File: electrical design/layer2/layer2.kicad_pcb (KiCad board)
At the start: 2 copper layers, 178 x 168.1 mm, 47 parts, among them J1 Conn_01x01_Female, J10 Conn_01x01_Female, J11 SH1.0 3P, J12 XH2.54 3P, J13 XT60-F, J14 XH2.54 2P, J15 XT60-F, J16 XT60-F, J17 SH1.0 2P, J18 Conn_01x01_Female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

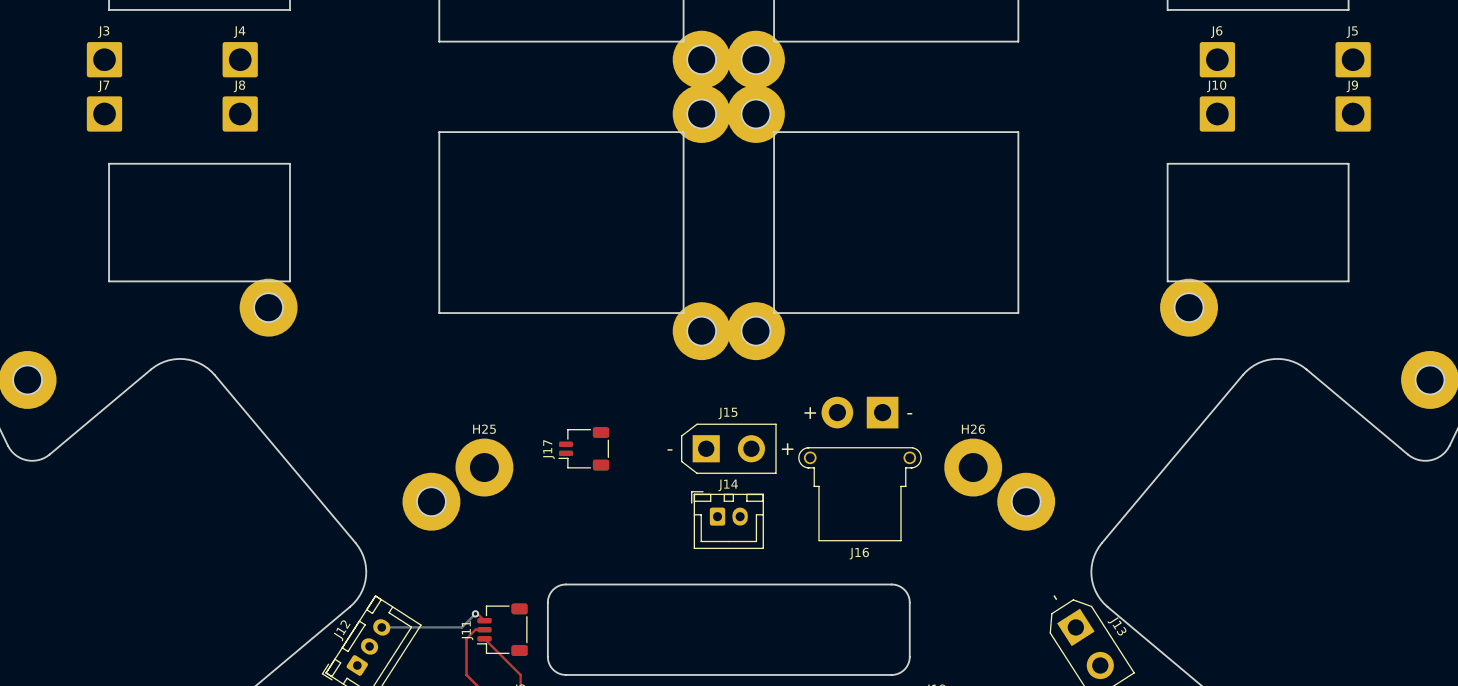
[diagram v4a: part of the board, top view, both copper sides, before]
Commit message: add pwm pullup resistor to rpi fan connector
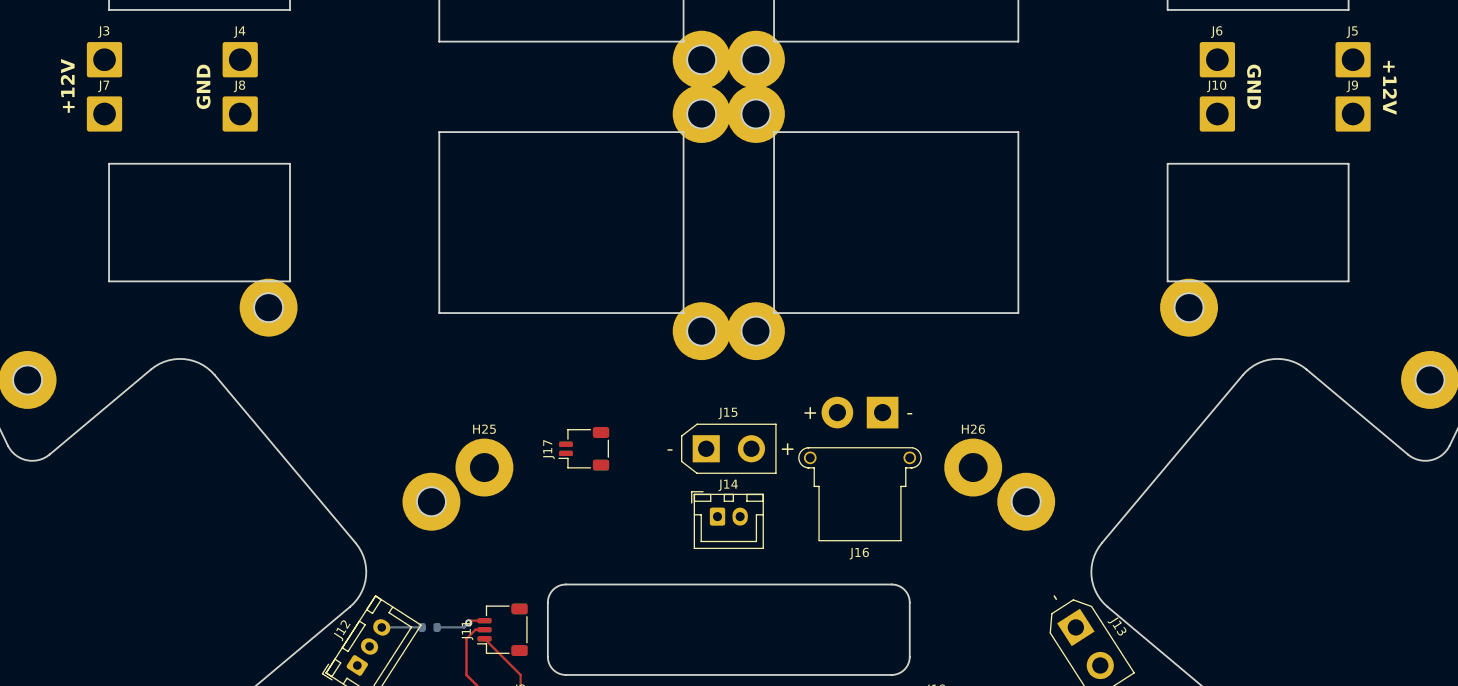
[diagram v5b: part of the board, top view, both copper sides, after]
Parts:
- added R1: 10k, Resistor_SMD:R_0603_1608Metric, B.Cu at (71.9, 164.8)
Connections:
- J12 pad 3: +3V3 -> Net-(J12-Pin_3)
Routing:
- net +3V3: track 12.3 -> 6.26 mm
- net Net-(J12-Pin_3): track 0.00 -> 4.46 mm
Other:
- board text added: "+12V"
- board text added: "GND"
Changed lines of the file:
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@@
   (net 3 "/BATT")
   (net 4 "+3V3")
+  (net 5 "Net-(J12-Pin_3)")
   (footprint "Connector_AMASS:AMASS_XT30UPB-F_1x02_P5.0mm_Vertical" (layer "F.Cu")
     (at 143.357043 164.747279 -57.3)
@@
       (net 1 "+12V") (pinfunction "Pin_2") (pintype "passive"))
     (pad "3" thru_hole oval (at 5 0 57.301) (size 1.7 1.95) (drill 0.95) (layers "*.Cu" "*.Mask")
-      (net 4 "+3V3") (pinfunction "Pin_3") (pintype "passive"))
+      (net 5 "Net-(J12-Pin_3)") (pinfunction "Pin_3") (pintype "passive"))
     (model "${KICAD6_3DMODEL_DIR}/Connector_JST.3dshapes/JST_XH_B3B-XH-A_1x03_P2.50mm_Vertical.wrl"
       (offset (xyz 0 0 0))
@@
     )
   )
+  (footprint "Resistor_SMD:R_0603_1608Metric" (layer "B.Cu")
+    (at 71.925 164.75)
+    (descr "Resistor SMD 0603 (1608 Metric), square (rectangular) end terminal, IPC_7351 nominal, (Body size source: IPC-SM-782 page 72, https://www.pcb-3d.com/wordpress/wp-content/uploads/ipc-sm-782a_amendment_1_and_2.pdf), generated with kicad-footprint-generator")
+    (tags "resistor")
+    (property "Sheetfile" "layer2.kicad_sch")
+    (property "Sheetname" "")
+    (property "ki_description" "Resistor")
+    (property "ki_keywords" "R res resistor")
+    (attr smd)
+    (fp_text reference "R1" (at 0 1.43) (layer "B.SilkS")
+        (effects (font (size 1 1) (thickness 0.15)) (justify mirror))
+    )
+    (fp_text value "10k" (at 0 -1.43) (layer "B.SilkS")
+        (effects (font (size 1 1) (thickness 0.15)) (justify mirror))
+    )
+    (fp_text user "${REFERENCE}" (at 0 0) (layer "B.Fab")
+        (effects (font (size 0.4 0.4) (thickness 0.06)) (justify mirror))
+    )
+    (fp_line (start -0.237258 -0.5225) (end 0.237258 -0.5225)
+      (stroke (width 0.12) (type solid)) (layer "B.SilkS"))
+    (fp_line (start -0.237258 0.5225) (end 0.237258 0.5225)
+      (stroke (width 0.12) (type solid)) (layer "B.SilkS"))
+    (fp_line (start -1.48 -0.73) (end -1.48 0.73)
+      (stroke (width 0.05) (type solid)) (layer "B.CrtYd"))
+    (fp_line (start -1.48 0.73) (end 1.48 0.73)
+      (stroke (width 0.05) (type solid)) (layer "B.CrtYd"))
+    (fp_line (start 1.48 -0.73) (end -1.48 -0.73)
+      (stroke (width 0.05) (type solid)) (layer "B.CrtYd"))
+    (fp_line (start 1.48 0.73) (end 1.48 -0.73)
+      (stroke (width 0.05) (type solid)) (layer "B.CrtYd"))
+    (fp_line (start -0.8 -0.4125) (end -0.8 0.4125)
+      (stroke (width 0.1) (type solid)) (layer "B.Fab"))
+    (fp_line (start -0.8 0.4125) (end 0.8 0.4125)
+      (stroke (width 0.1) (type solid)) (layer "B.Fab"))
+    (fp_line (start 0.8 -0.4125) (end -0.8 -0.4125)
+      (stroke (width 0.1) (type solid)) (layer "B.Fab"))
+    (fp_line (start 0.8 0.4125) (end 0.8 -0.4125)
+      (stroke (width 0.1) (type solid)) (layer "B.Fab"))
+    (pad "1" smd roundrect (at -0.825 0) (size 0.8 0.95) (layers "B.Cu" "B.Paste" "B.Mask") (roundrect_rratio 0.25)
+      (net 5 "Net-(J12-Pin_3)") (pintype "passive"))
+    (pad "2" smd roundrect (at 0.825 0) (size 0.8 0.95) (layers "B.Cu" "B.Paste" "B.Mask") (roundrect_rratio 0.25)
+      (net 4 "+3V3") (pintype "passive"))
+    (model "${KICAD6_3DMODEL_DIR}/Resistor_SMD.3dshapes/R_0603_1608Metric.wrl"
+      (offset (xyz 0 0 0))
+      (scale (xyz 1 1 1))
+      (rotate (xyz 0 0 0))
+    )
+  )
   (gr_arc (start 25.330811 65.328595) (mid 27.404624 63.728825) (end 29.944652 64.3677)
     (stroke (width 0.2) (type solid)) (layer "Edge.Cuts"))
@@
   (gr_line (start 158.048228 171.859363) (end 146.853507 162.465877)
     (stroke (width 0.2) (type solid)) (layer "Edge.Cuts"))
+  (gr_text "GND" (at 47 105 90) (layer "F.SilkS")
+    (effects (font (size 1.5 1.5) (thickness 0.3) bold))
+  )
+  (gr_text "+12V" (at 32 105 90) (layer "F.SilkS")
+    (effects (font (size 1.5 1.5) (thickness 0.3) bold))
+  )
+  (gr_text "GND" (at 163 105 -90) (layer "F.SilkS")
+    (effects (font (size 1.5 1.5) (thickness 0.3) bold))
+  )
+  (gr_text "+12V" (at 178 105 -90) (layer "F.SilkS")
+    (effects (font (size 1.5 1.5) (thickness 0.3) bold))
+  )
   (segment (start 78 166) (end 82 170) (width 0.25) (layer "F.Cu") (net 2))
   (segment (start 78 165) (end 77 165) (width 0.25) (layer "F.Cu") (net 2))
@@
   (segment (start 76 170) (end 81 175) (width 0.25) (layer "F.Cu") (net 2))
   (segment (start 77 165) (end 76 166) (width 0.25) (layer "F.Cu") (net 2))
-  (segment (start 77 163.25) (end 77.25 163.25) (width 0.25) (layer "F.Cu") (net 4))
-  (segment (start 77.25 163.25) (end 78 164) (width 0.25) (layer "F.Cu") (net 4))
-  (via (at 77 163.25) (size 0.8) (drill 0.4) (layers "F.Cu" "B.Cu") (net 4))
-  (segment (start 66.642957 164.74728) (end 75.50272 164.74728) (width 0.25) (layer "B.Cu") (net 4))
-  (segment (start 75.50272 164.74728) (end 77 163.25) (width 0.25) (layer "B.Cu") (net 4))
+  (segment (start 78 164) (end 76.5 164) (width 0.25) (layer "F.Cu") (net 4))
+  (segment (start 76.5 164) (end 76.25 164.25) (width 0.25) (layer "F.Cu") (net 4))
+  (via (at 76.25 164.25) (size 0.8) (drill 0.4) (layers "F.Cu" "B.Cu") (net 4))
+  (segment (start 76.25 164.25) (end 75.75 164.75) (width 0.25) (layer "B.Cu") (net 4))
+  (segment (start 76.25 164.25) (end 75.75272 164.74728) (width 0.25) (layer "B.Cu") (net 4))
+  (segment (start 75.75 164.75) (end 72.75 164.75) (width 0.25) (layer "B.Cu") (net 4))
+  (segment (start 71.1 164.75) (end 66.645677 164.75) (width 0.25) (layer "B.Cu") (net 5))
+  (segment (start 66.645677 164.75) (end 66.642957 164.74728) (width 0.25) (layer "B.Cu") (net 5))
   (zone (net 1) (net_name "+12V") (layer "F.Cu") (hatch edge 0.508)
     (connect_pads yes (clearance 0.508))

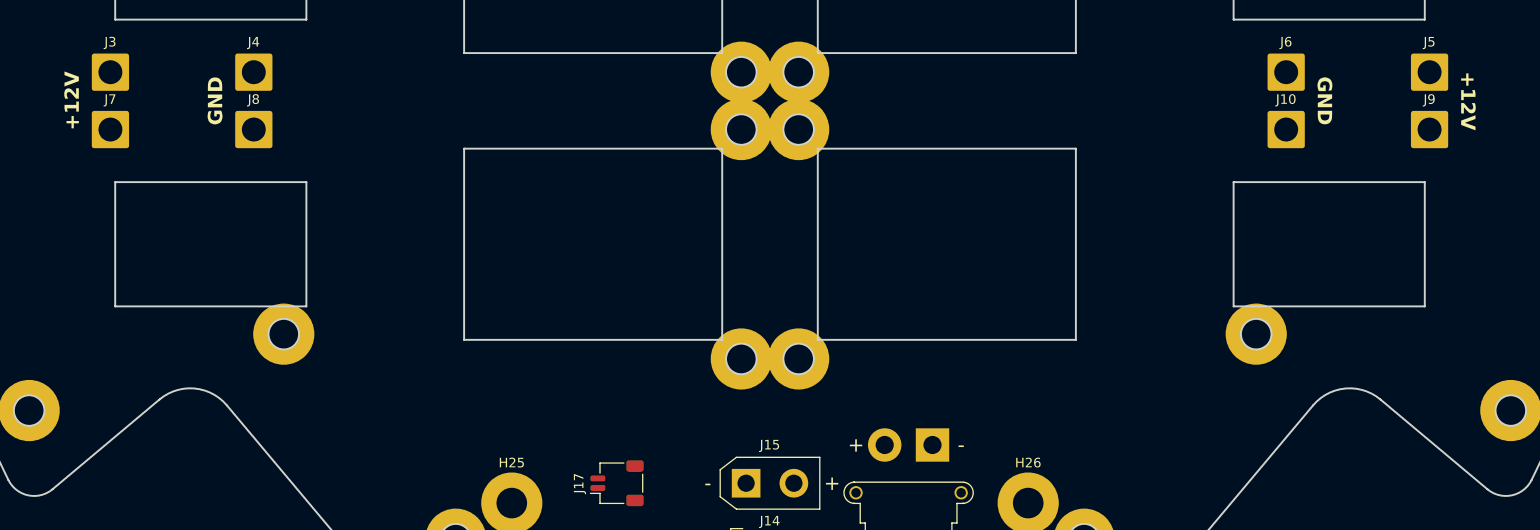
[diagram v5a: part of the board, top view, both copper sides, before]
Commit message: reposition motor power ports
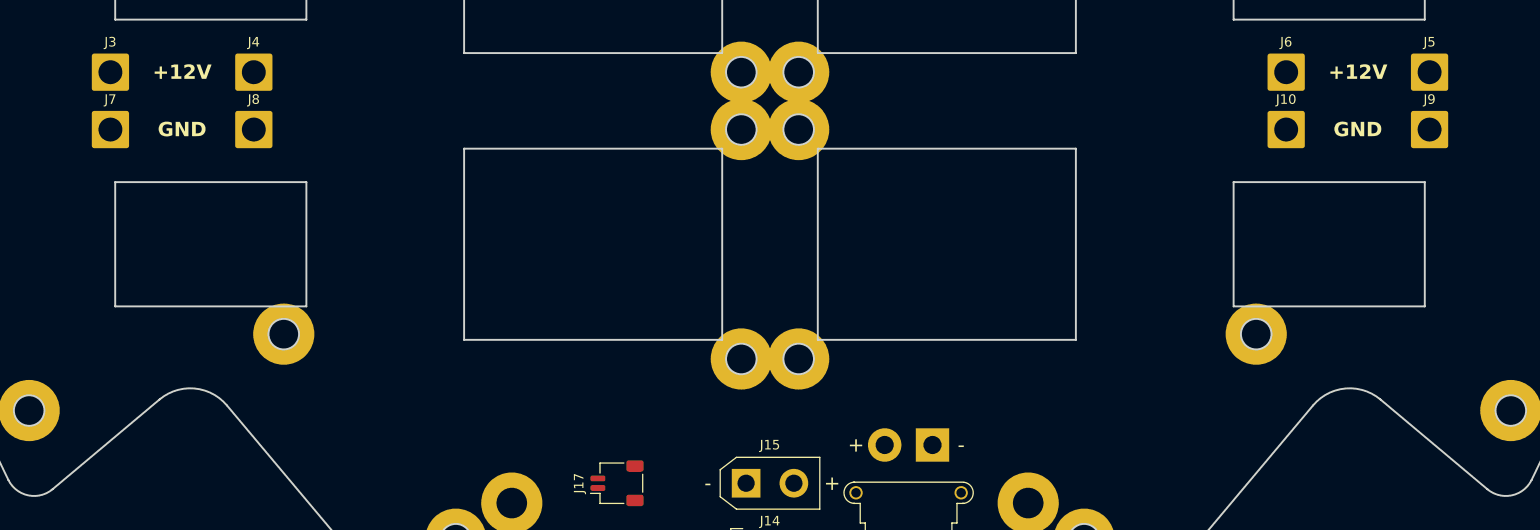
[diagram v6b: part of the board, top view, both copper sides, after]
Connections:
- J4 pad 1: GND -> +12V
- J6 pad 1: GND -> +12V
- J7 pad 1: +12V -> GND
- J9 pad 1: +12V -> GND

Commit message: resolve some l2 and l3 board issues
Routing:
- net GND: track 25.1 -> 27.1 mm, vias 0 -> 1
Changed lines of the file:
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@@
     (property "ki_keywords" "connector")
     (attr exclude_from_pos_files)
-    (fp_text reference "J18" (at 0 -3.4) (layer "F.SilkS")
+    (fp_text reference "J18" (at 0 3.5) (layer "F.SilkS")
         (effects (font (size 1 1) (thickness 0.15)))
     )
@@
     (property "ki_keywords" "connector")
     (attr exclude_from_pos_files)
-    (fp_text reference "J1" (at 0 -3.4) (layer "F.SilkS")
+    (fp_text reference "J1" (at 0 3.5) (layer "F.SilkS")
         (effects (font (size 1 1) (thickness 0.15)))
     )
@@
     (effects (font (size 1.5 1.5) (thickness 0.3) bold))
   )
+  (segment (start 87 144.5) (end 87 145.5) (width 0.25) (layer "F.Cu") (net 2))
   (segment (start 78 166) (end 82 170) (width 0.25) (layer "F.Cu") (net 2))
   (segment (start 78 165) (end 77 165) (width 0.25) (layer "F.Cu") (net 2))
@@
   (segment (start 82 170) (end 82 171.25) (width 0.25) (layer "F.Cu") (net 2))
   (segment (start 76 170) (end 81 175) (width 0.25) (layer "F.Cu") (net 2))
+  (segment (start 87 145.5) (end 87 146.5) (width 0.25) (layer "F.Cu") (net 2))
   (segment (start 77 165) (end 76 166) (width 0.25) (layer "F.Cu") (net 2))
+  (via (at 87 146.5) (size 0.8) (drill 0.4) (layers "F.Cu" "B.Cu") (net 2))
   (segment (start 78 164) (end 76.5 164) (width 0.25) (layer "F.Cu") (net 4))
   (segment (start 76.5 164) (end 76.25 164.25) (width 0.25) (layer "F.Cu") (net 4))

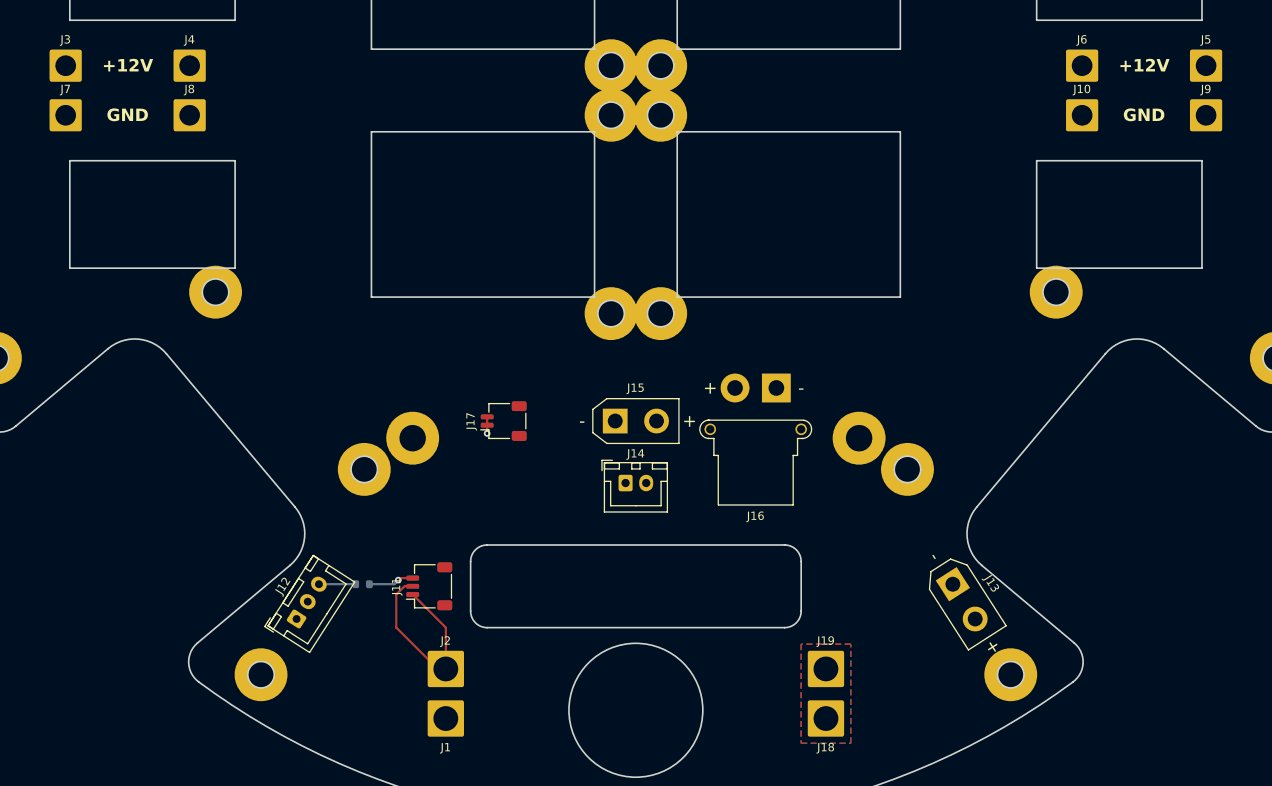
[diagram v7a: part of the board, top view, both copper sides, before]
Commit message: add jlc order number silkscreen
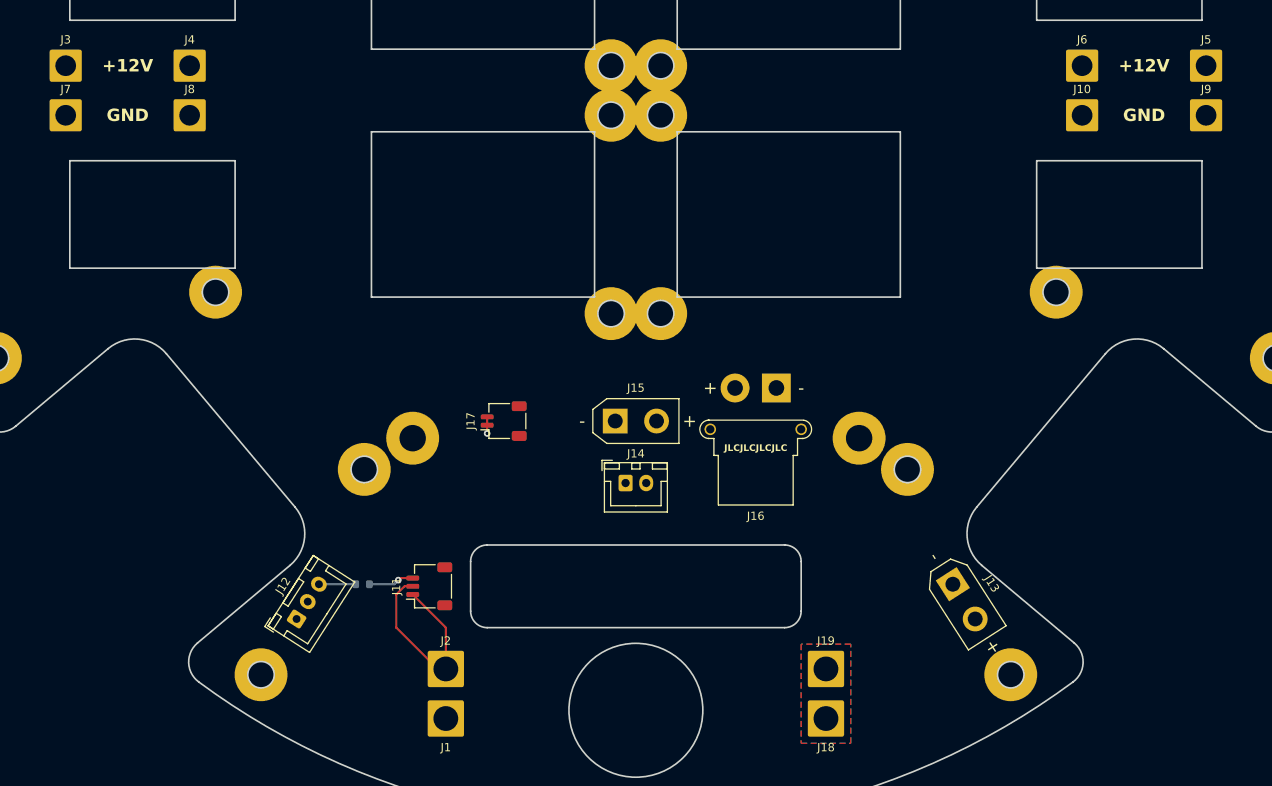
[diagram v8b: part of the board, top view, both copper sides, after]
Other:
- board text added: "JLCJLCJLCJLC"
